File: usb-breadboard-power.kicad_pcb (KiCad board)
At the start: 2 copper layers, 53 x 25.7 mm, 39 parts, among them J1 USB_C_Receptacle_PowerOnly_6P, J2 Conn_02x02_Counter_Clockwise, J3 Conn_02x02_Counter_Clockwise, Q3 Q_Dual_NMOS, SW1 SW_DIP_x03, U2 BD33FC0FP, U3 LM339

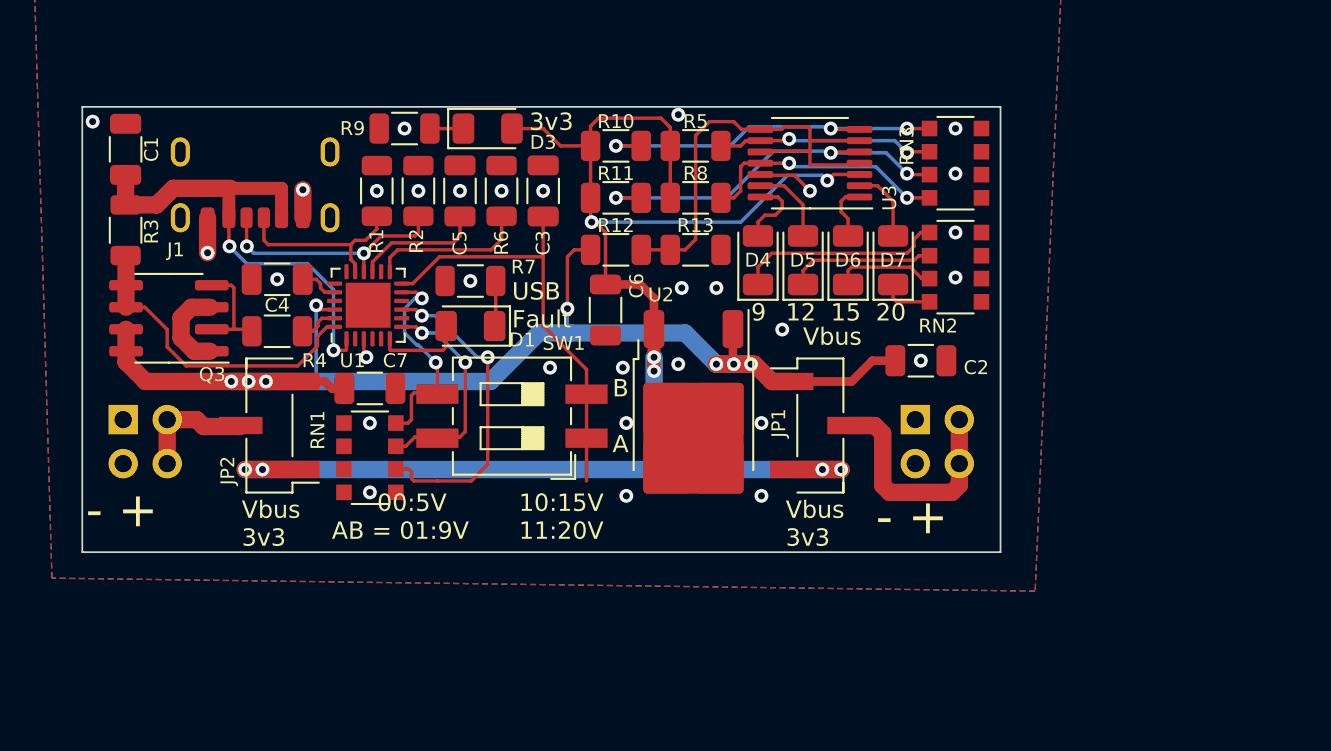
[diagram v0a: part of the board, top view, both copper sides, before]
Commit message: Swapped IC to one that supports 12v
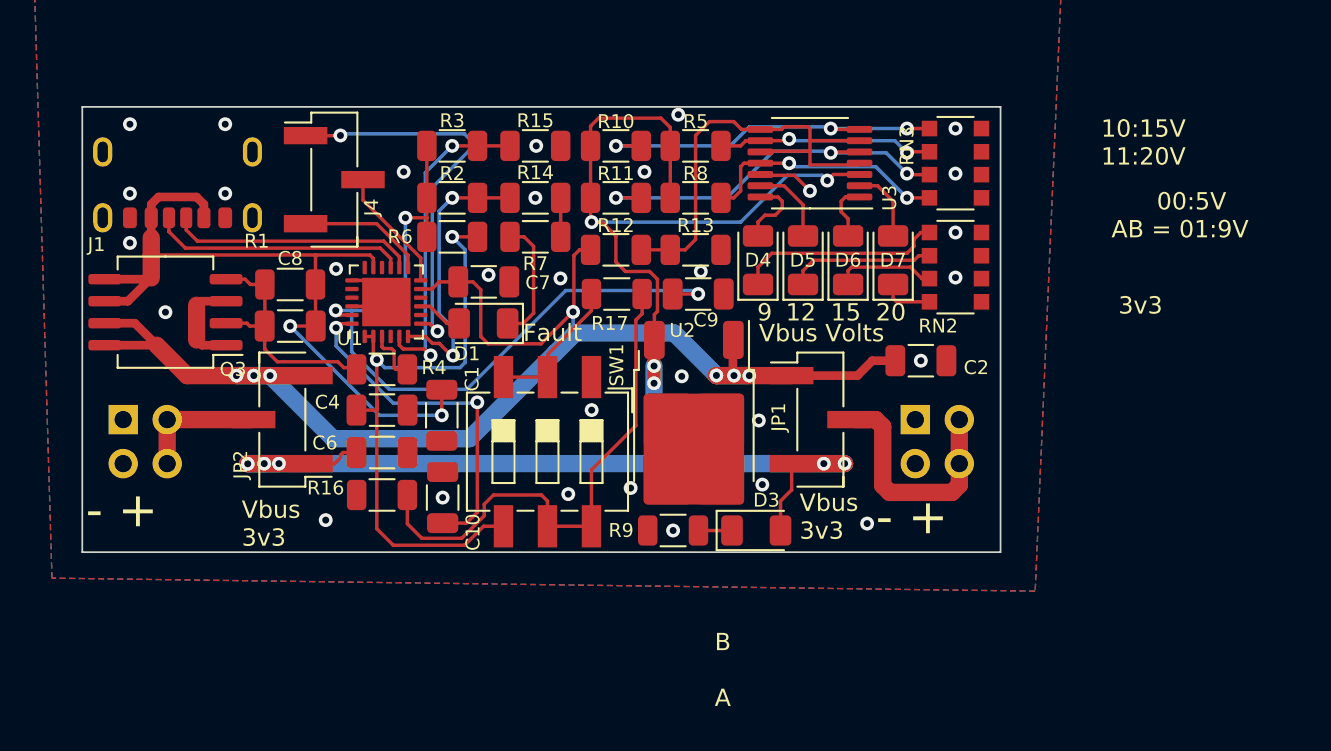
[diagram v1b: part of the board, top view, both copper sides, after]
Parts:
- removed C3, C5: 0.1u, Capacitor_SMD:C_1206_3216Metric
- removed RN1: 100k, Resistor_SMD:R_Array_Convex_4x1206
- added C10: 1u, Capacitor_SMD:C_1206_3216Metric, F.Cu at (104.8, 106.1)
- added C8: 1u, Capacitor_SMD:C_1206_3216Metric, F.Cu at (96.0, 96.2)
- added C9: 1u, Capacitor_SMD:C_1206_3216Metric, F.Cu at (119.5, 94.3)
- added J4: Conn_01x03, Connector_PinHeader_2.54mm:PinHeader_1x03_P2.54mm_Vertical_SMD_Pin1Left, F.Cu at (98.5, 87.8)
- added R14: R, Resistor_SMD:R_1206_3216Metric, F.Cu at (110.2, 88.8)
- added R15: R, Resistor_SMD:R_1206_3216Metric, F.Cu at (110.2, 85.8)
- added R16: 1k2, Resistor_SMD:R_1206_3216Metric, F.Cu at (101.3, 106.0)
- added R17: 3k, Resistor_SMD:R_1206_3216Metric, F.Cu at (114.8, 94.3)
- Q3: value Q_Dual_NMOS -> DMP6110; footprint Package_SO:SOIC-8_3.9x4.9mm_P1.27mm -> Package_SO:SO-8_5.3x6.2mm_P1.27mm
- R1: value 5k1 -> 10k
- R2: value 5k1 -> R
- R3: value 10m -> R
- R6: value 36k -> 5k1
- SW1: footprint Button_Switch_SMD:SW_DIP_SPSTx02_Slide_6.7x6.64mm_W8.61mm_P2.54mm_LowProfile -> Button_Switch_SMD:SW_DIP_SPSTx03_Slide_6.7x9.18mm_W8.61mm_P2.54mm_LowProfile
- U1: value ~ -> CYPD3177; footprint Package_DFN_QFN:WQFN-24-1EP_4x4mm_P0.5mm_EP2.6x2.6mm -> Package_DFN_QFN:QFN-24-1EP_4x4mm_P0.5mm_EP2.8x2.8mm
- moved D3 27.9 mm to (122.9, 108.0)
- moved R9 27.9 mm to (118.1, 108.0)
- moved C1 23.8 mm to (104.8, 101.3), turned to -90 degrees
- moved R3 19.5 mm to (105.3, 85.8), turned to 0 degrees
- moved C6 15.3 mm to (101.3, 103.5), turned to 0 degrees
- moved C4 9.67 mm to (101.3, 101.0), turned to 0 degrees
- moved C7 9.00 mm to (107.2, 93.7)
- moved R1 7.36 mm to (96.0, 93.8), turned to 180 degrees
- moved R4 6.44 mm to (101.3, 98.7)
- moved R7 4.53 mm to (110.2, 91.0), turned to 0 degrees
- moved J1 4.48 mm to (89.5, 90.0)
- moved R6 3.89 mm to (105.3, 91.0), turned to 0 degrees
- moved SW1 2.90 mm to (110.8, 103.5), turned to -90 degrees
- moved R2 1.99 mm to (105.3, 88.8), turned to 0 degrees
- moved U1 1.07 mm to (101.5, 94.8)
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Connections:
- C1 pad 1: Net-(U1-ISENP) -> Net-(U1-VBUS_IN)
- C4 pad 1: Net-(U1-V5V) -> Net-(U1-Vbus_Max)
- J1 pad A9: Net-(U1-ISENP) -> Net-(U1-VBUS_IN)
- J1 pad B9: Net-(U1-ISENP) -> Net-(U1-VBUS_IN)
- Q3 pad 5: Net-(U1-VCC) -> Net-(U1-VBUS_IN)
- Q3 pad 6: Net-(U1-VCC) -> Net-(U1-VBUS_IN)
- R1 pad 1: Net-(J1-CC1) -> Net-(U1-VBUS_IN)
- R1 pad 2: GND -> Net-(Q3A-G)
- R2 pad 1: Net-(J1-CC2) -> Net-(U1-VDDD)
- R2 pad 2: GND -> Net-(U1-Isink_Fine)
- R3 pad 1: Net-(U1-ISENP) -> Net-(U1-VDDD)
- R3 pad 2: Net-(U1-VCC) -> Net-(U1-Isink_Course)
- R4 pad 1: Net-(U1-PWR_EN) -> Net-(U1-Vbus_Fet_En)
- R6 pad 1: Net-(U1-PSEL) -> Net-(U1-VDDD)
- R6 pad 2: GND -> Net-(U1-Vbus_Max)
- SW1 pad 1: Net-(U1-V3VD) -> GND
- SW1 pad 2: Net-(U1-V3VD) -> Net-(R17-Pad2)
- SW1 pad 3: Net-(RN1-R2.2) -> Net-(R17-Pad2)
- SW1 pad 4: Net-(RN1-R3.2) -> Net-(U1-Vbus_Max)
- U1 pad 1: Net-(U1-ISENP) -> Net-(U1-Vbus_Max)
- U1 pad 10: (no net) -> unconnected-(U1-FLIP-Pad10)
- U1 pad 11: Net-(RN1-R1.2) -> VBUS
- U1 pad 12: Net-(U1-V3VD) -> Net-(J4-Pin_2)
- U1 pad 13: Net-(U1-PSEL) -> Net-(J4-Pin_3)
- U1 pad 14: unconnected-(U1-VFB-Pad14) -> Net-(J1-CC1)
- U1 pad 15: Net-(U1-IFB) -> Net-(J1-CC2)
- U1 pad 16: Net-(J1-CC2) -> unconnected-(U1-D--Pad16)
- U1 pad 17: Net-(J1-CC1) -> Net-(U1-VBUS_IN)
- U1 pad 19: (no net) -> GND
- U1 pad 2: (no net) -> Net-(U1-Vbus_Max)
- U1 pad 20: Net-(U1-V5V) -> unconnected-(U1-DNU1-Pad20)
- U1 pad 21: (no net) -> unconnected-(U1-DNU2-Pad21)
- U1 pad 22: VBUS -> GND
- U1 pad 23: Net-(U1-PWR_EN) -> Net-(U1-VDDD)
- U1 pad 24: Net-(U1-VCC) -> Net-(U1-VCCD)
- U1 pad 25: (no net) -> GND
- U1 pad 3: GND -> Net-(U1-Vbus_Fet_En)
- U1 pad 4: (no net) -> unconnected-(U1-Safe_Pwr_En-Pad4)
- U1 pad 5: (no net) -> Net-(U1-Isink_Course)
- U1 pad 6: Net-(D1-A) -> Net-(U1-Isink_Fine)
- U1 pad 7: Net-(RN1-R2.2) -> Net-(J4-Pin_1)
- U1 pad 9: Net-(RN1-R3.2) -> Net-(D1-A)
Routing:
- net Net-(U1-VBUS_IN): track 0.00 -> 48.3 mm, vias 0 -> 2
- net Net-(U1-VDDD): track 0.00 -> 43.2 mm, vias 0 -> 3
- net Net-(U1-Vbus_Max): track 0.00 -> 36.2 mm, vias 0 -> 2
- net Net-(R16-Pad2): track 0.00 -> 30.3 mm
- net Net-(U1-ISENP): track 28.3 -> 0.00 mm, vias 2 -> 0
- net Net-(U1-V3VD): track 25.1 -> 0.00 mm
- net Net-(J4-Pin_1): track 0.00 -> 23.1 mm, vias 0 -> 2
- net Net-(U1-VCCD): track 0.00 -> 20.3 mm, vias 0 -> 2
- net Net-(U1-Isink_Course): track 0.00 -> 18.6 mm, vias 0 -> 2
- net Net-(RN1-R3.2): track 18.5 -> 0.00 mm, vias 2 -> 0
- net Net-(U1-VCC): track 18.3 -> 0.00 mm
- net Net-(U1-Isink_Fine): track 0.00 -> 16.1 mm, vias 0 -> 2
- net Net-(RN1-R2.2): track 12.9 -> 0.00 mm, vias 2 -> 0
- net Net-(RN1-R1.2): track 12.2 -> 0.00 mm, vias 2 -> 0
- net VBUS: track 71.8 -> 83.7 mm, vias 8 -> 7
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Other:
- board text added: "Fault"
- board text added: "Vbus Volts"
- board text removed: "USB Fault"
- board text removed: "Vbus"

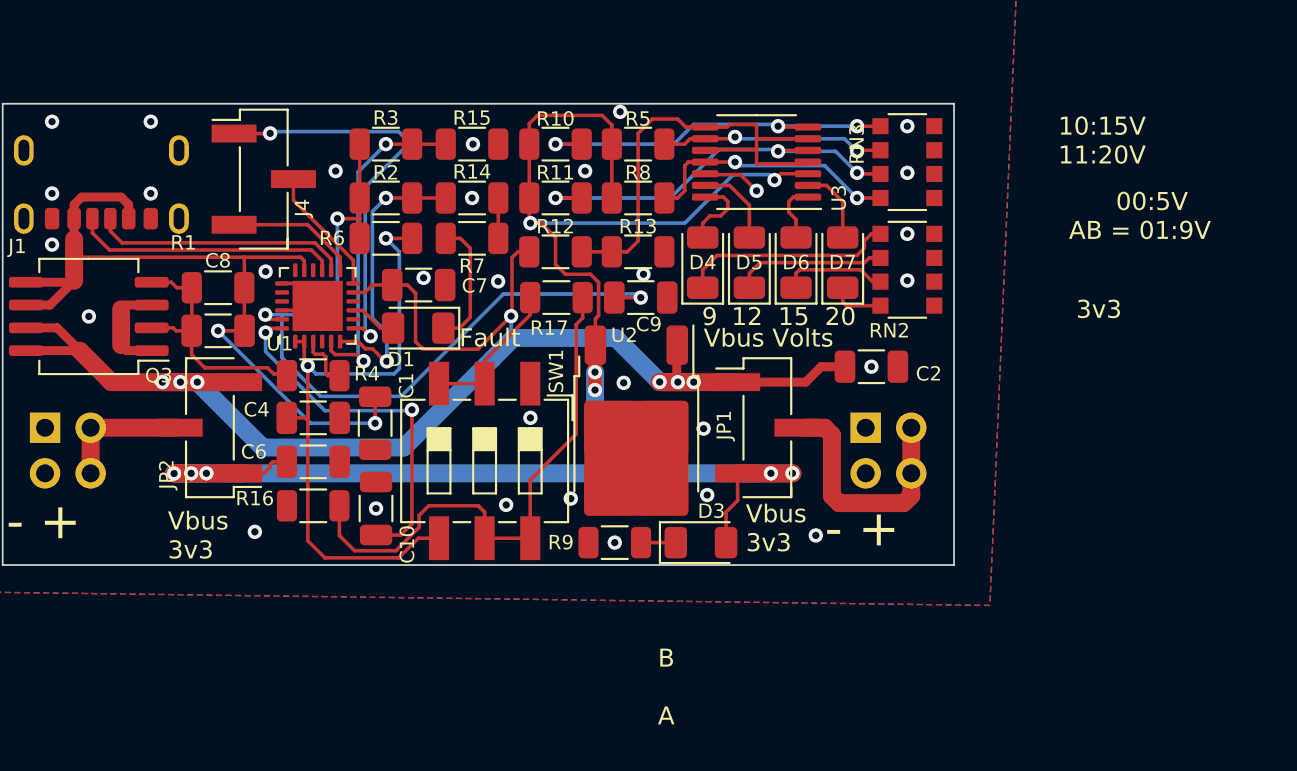
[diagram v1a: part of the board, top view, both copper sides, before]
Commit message: Cleaned up schematic and added Vbus LED
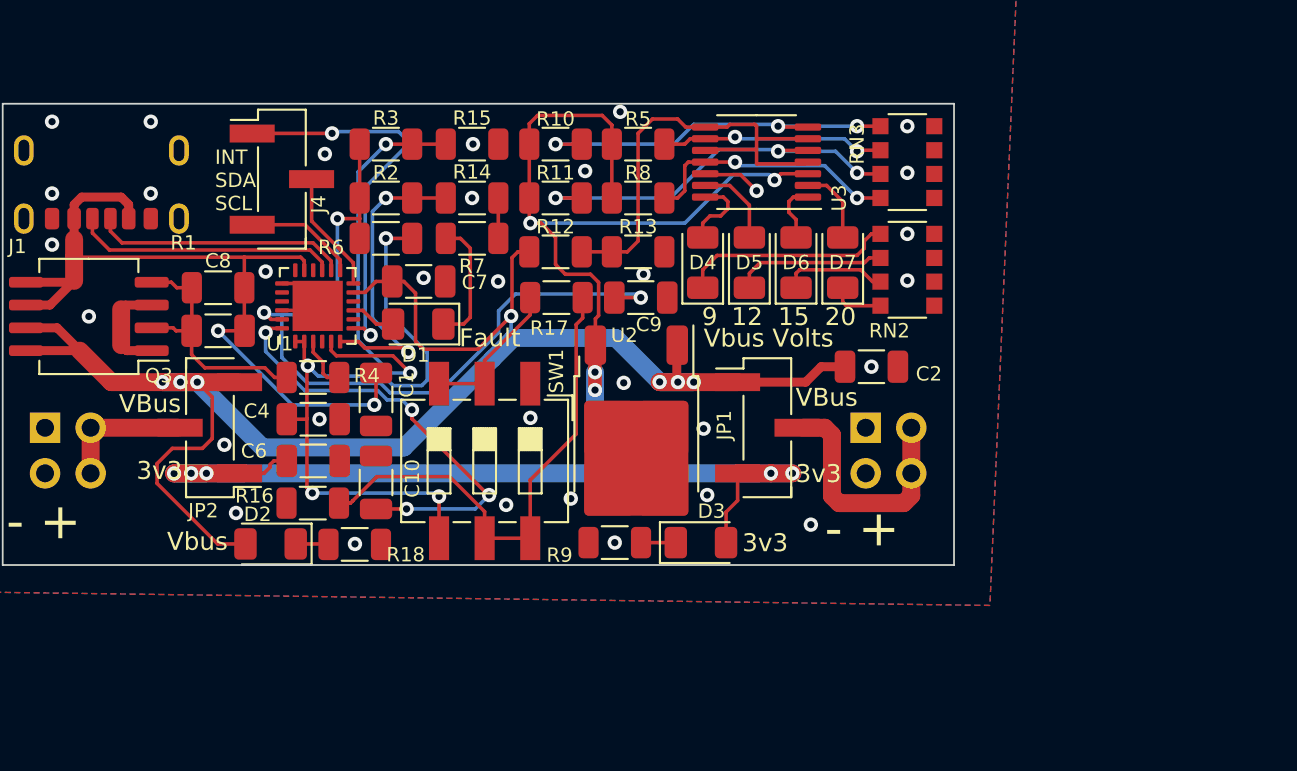
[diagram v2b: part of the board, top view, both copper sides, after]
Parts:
- added D2: LED, LED_SMD:LED_1206_3216Metric, F.Cu at (98.9, 108.1)
- added R18: R, Resistor_SMD:R_1206_3216Metric, F.Cu at (103.6, 108.1)
- J2, J3: value Conn_02x02_Counter_Clockwise -> Conn_02x02
- moved C10 1.45 mm to (104.8, 104.7)
- moved C1 1.33 mm to (104.8, 100.0)
- moved J4 1.01 mm to (99.6, 87.8)
- moved D1 0.22 mm to (107.2, 95.8)
- moved C7 0.20 mm to (107.2, 93.5)
- moved R16 0.15 mm to (101.3, 105.8)
- moved R4 0.10 mm to (101.3, 98.8)
- moved C4 0.08 mm to (101.3, 101.1)
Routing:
- net VBUS: track 83.7 -> 98.4 mm
- net Net-(U1-Isink_Course): track 18.6 -> 23.9 mm
- net Net-(U1-VCCD): track 20.3 -> 25.0 mm, vias 2 -> 4
- net Net-(R16-Pad2): track 30.3 -> 28.2 mm
- net Net-(D2-K): track 0.00 -> 1.84 mm
- net Net-(U1-Vbus_Max): track 36.2 -> 37.6 mm, vias 2 -> 4
- net Net-(U1-Isink_Fine): track 16.1 -> 17.2 mm
- net Net-(U1-VDDD): track 43.2 -> 43.9 mm
- net GND: vias 31 -> 33
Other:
- board text added: "INT SDA SCL"
- board text added: "VBus"
- board text added: "Vbus"
- board text removed: "00:5V AB = 01:9V"
- board text removed: "10:15V 11:20V"
- board text removed: "B A"
- board text removed: "Vbus 3v3"

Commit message: Updated Mouser BOM
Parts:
- J1: footprint usb-breadboard:usbc -> usb-breadboard:J-Amphenol-USB-C
- moved J1 3.00 mm to (89.5, 87.0)
- moved J2 1.02 mm to (87.4, 101.6)
- moved J3 1.01 mm to (131.1, 101.6)
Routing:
- net GND: track 10.0 -> 7.91 mm, vias 33 -> 34
- net Net-(J4-Pin_1): track 22.9 -> 20.9 mm
- net Net-(J3-Pin_3): track 13.7 -> 12.3 mm
- net Net-(J2-Pin_3): track 7.39 -> 6.37 mm

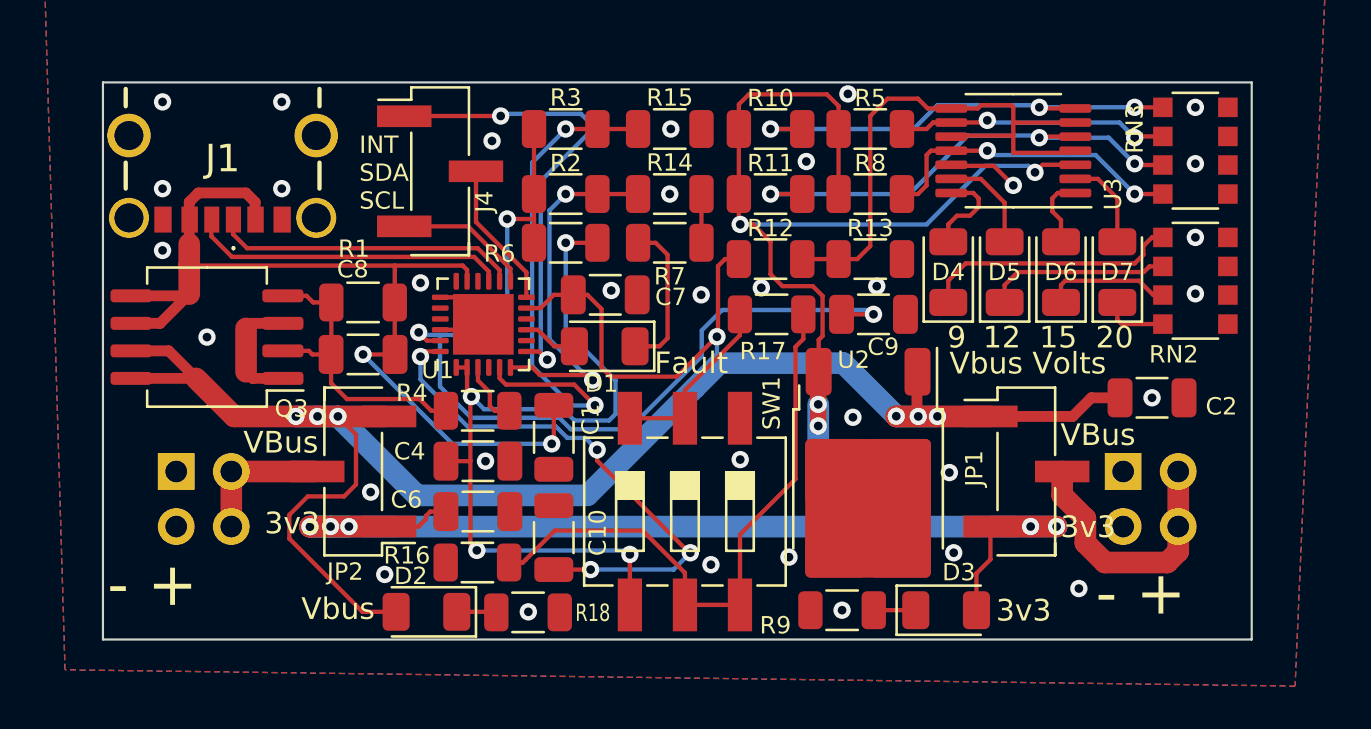
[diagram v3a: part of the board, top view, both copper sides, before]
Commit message: Updated gitignore and added fuse
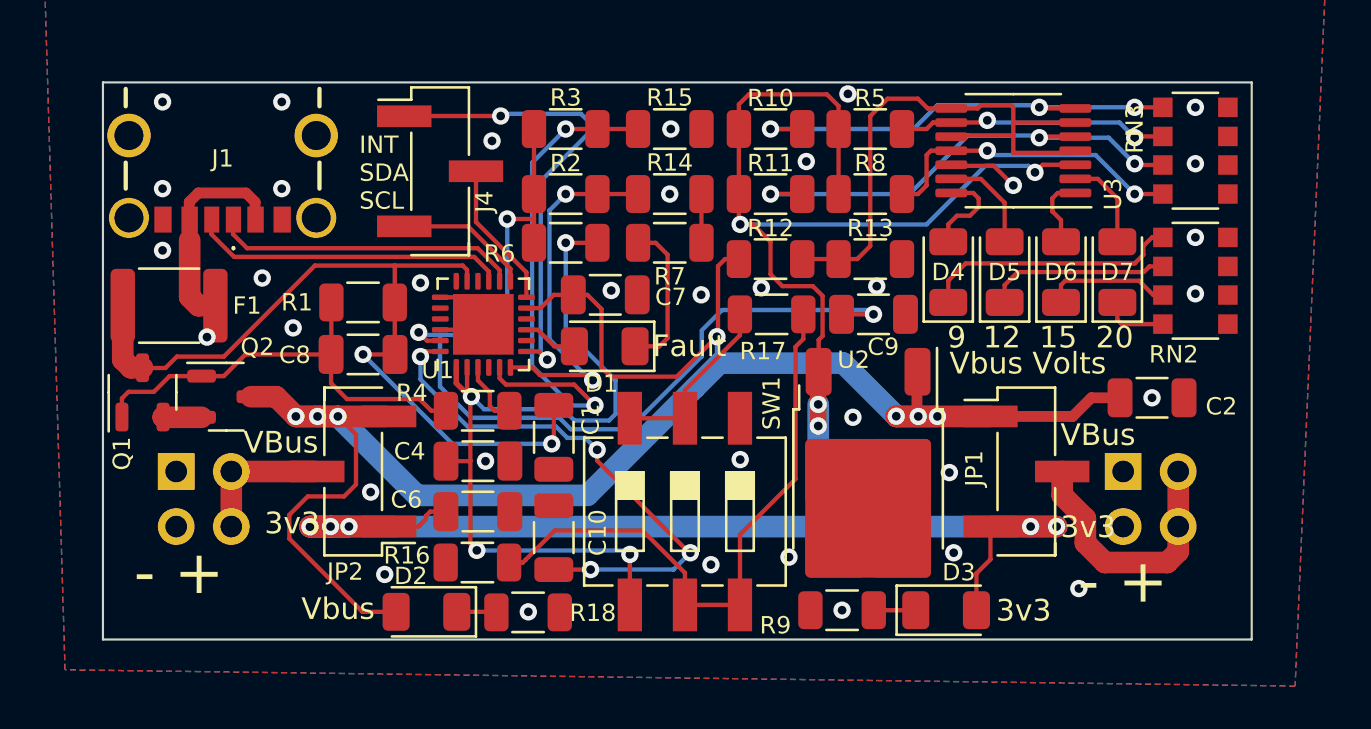
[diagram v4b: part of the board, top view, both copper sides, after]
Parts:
- removed Q3: DMP6110, Package_SO:SO-8_5.3x6.2mm_P1.27mm
- added F1: Fuse, Fuse:Fuse_1812_4532Metric, F.Cu at (87.0, 94.0)
- added Q1: Q_PMOS_GSD, Package_TO_SOT_SMD:SOT-23-3, F.Cu at (85.8, 98.0)
- added Q2: Q_PMOS_GSD, Package_TO_SOT_SMD:SOT-23-3, F.Cu at (89.7, 98.2)
- R14: value R -> 0
- R15: value R -> 2k2
- R18, R3: value R -> 5k1
- R2: value R -> DNP
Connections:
- C1 pad 1: Net-(U1-VBUS_IN) -> Net-(Q1-D)
- C8 pad 1: Net-(U1-VBUS_IN) -> Net-(Q1-D)
- J1 pad A9: Net-(U1-VBUS_IN) -> Net-(F1-Pad1)
- J1 pad B9: Net-(U1-VBUS_IN) -> Net-(F1-Pad1)
- R1 pad 1: Net-(U1-VBUS_IN) -> Net-(Q1-D)
- U1 pad 17: Net-(U1-VBUS_IN) -> Net-(Q1-D)
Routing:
- net Net-(U1-VBUS_IN): track 48.1 -> 0.00 mm, vias 2 -> 0
- net Net-(Q1-D): track 0.00 -> 39.1 mm, vias 0 -> 2
- net Net-(F1-Pad1): track 0.00 -> 9.96 mm
- net VBUS: track 98.4 -> 89.0 mm
- net Net-(Q1-G): track 13.9 -> 20.6 mm
- net Net-(Q3A-S): track 5.62 -> 0.00 mm
- net Net-(Q1-S): track 0.00 -> 1.78 mm
- net Net-(U1-Vbus_Max): track 37.3 -> 38.5 mm
- net GND: vias 34 -> 36
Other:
- board text added: "V1.0"

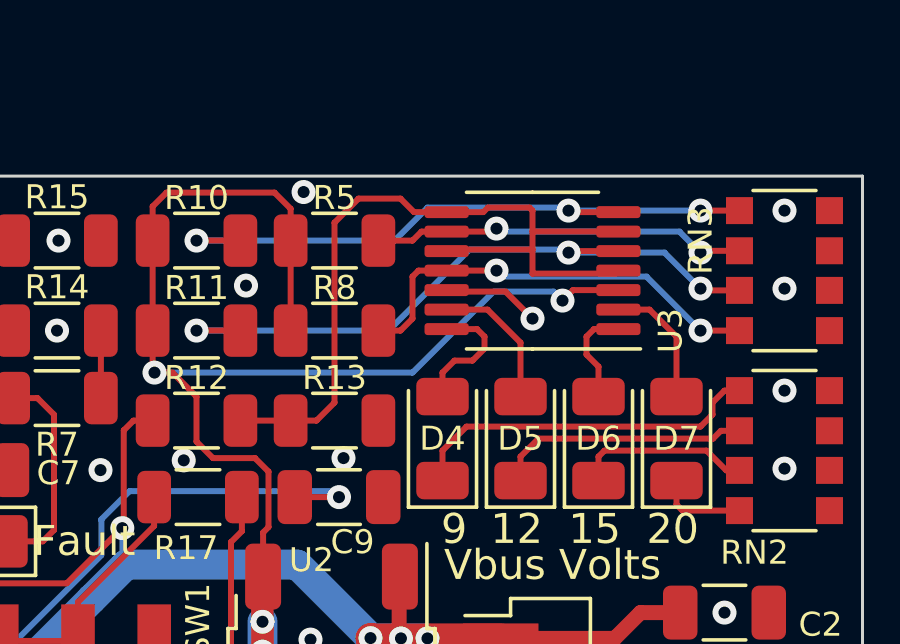
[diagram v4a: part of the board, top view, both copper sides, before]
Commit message: Moved voltage LED refdes out from under diodes
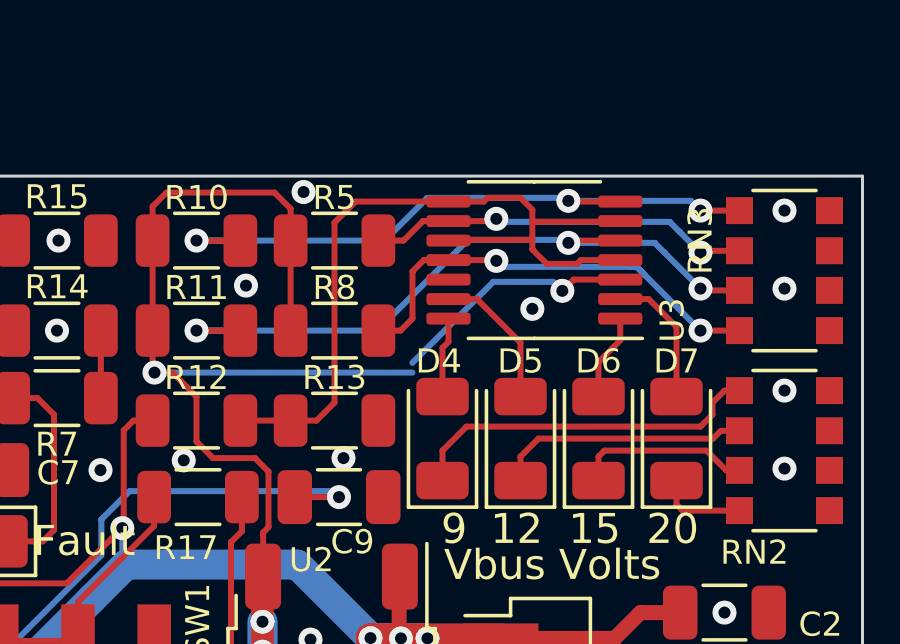
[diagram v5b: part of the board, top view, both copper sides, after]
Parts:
- moved U3 0.36 mm to (126.1, 86.5)
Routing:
- net GND: track 7.91 -> 4.72 mm
- net Net-(D4-A): track 4.30 -> 2.68 mm
- net Net-(RN3-R4.1): track 14.5 -> 15.5 mm
